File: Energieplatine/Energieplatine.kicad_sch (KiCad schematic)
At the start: 22 parts, among them J1 USB_C_Receptacle_PowerOnly_6P, J2 Conn_01x02_Pin, U1 4027, U2 TL072, U3 LM2576HVT-ADJ, U4 LM2577T-ADJ

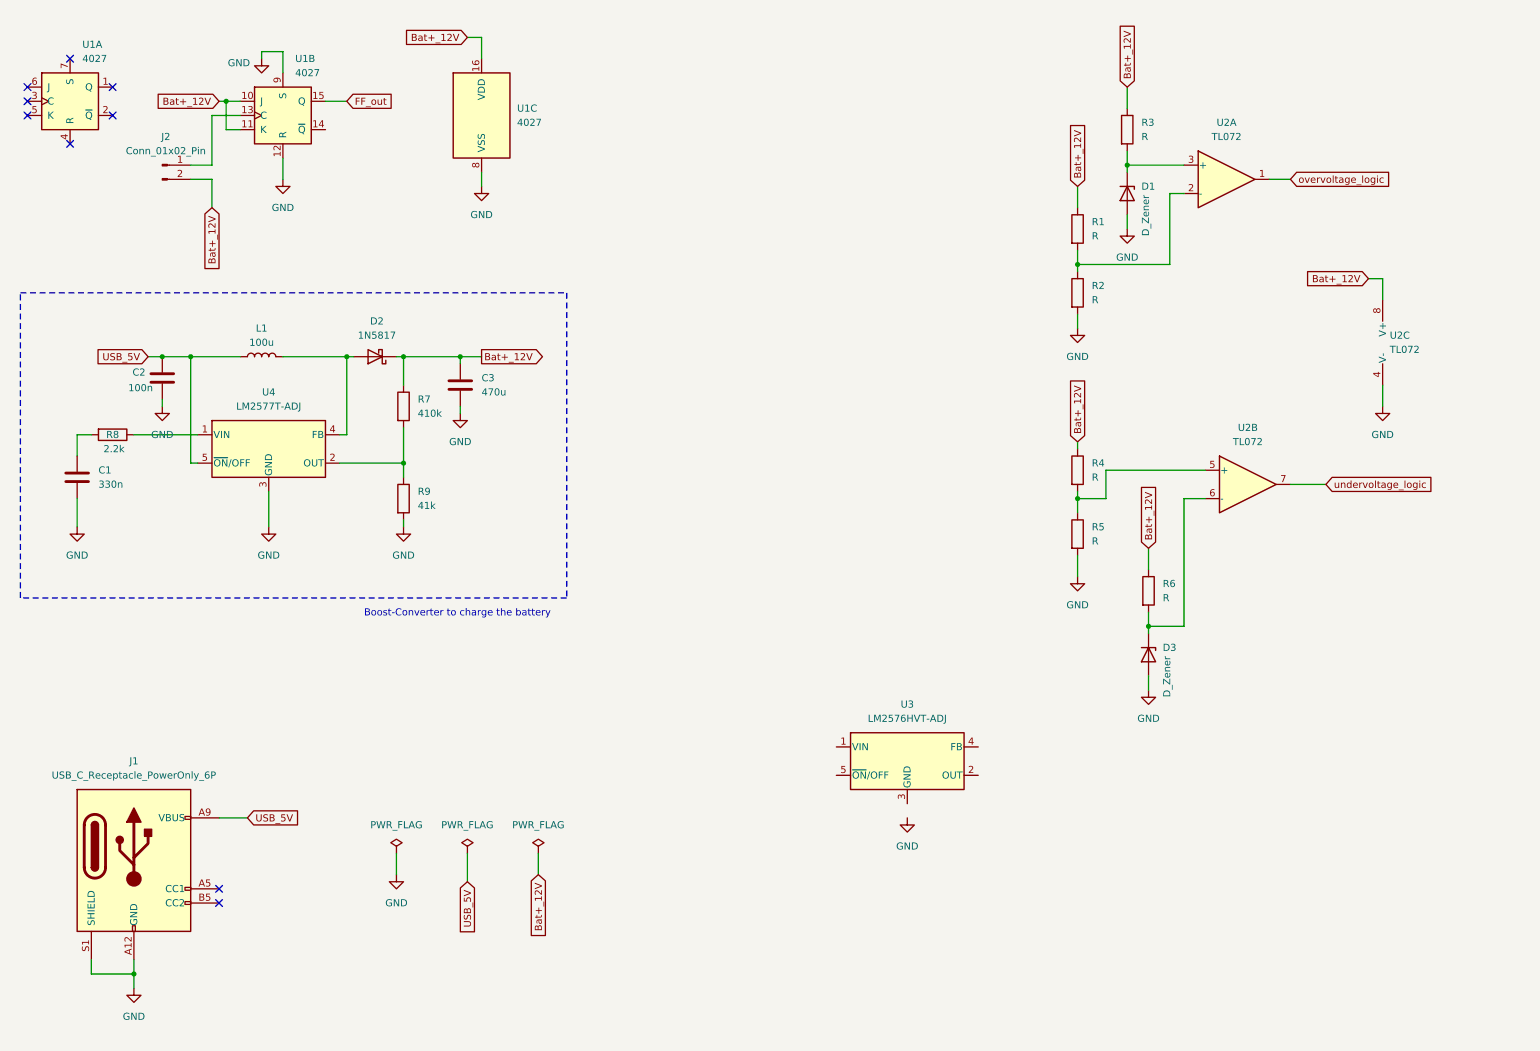
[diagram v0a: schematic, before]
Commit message: Layout is has no DRC errors.
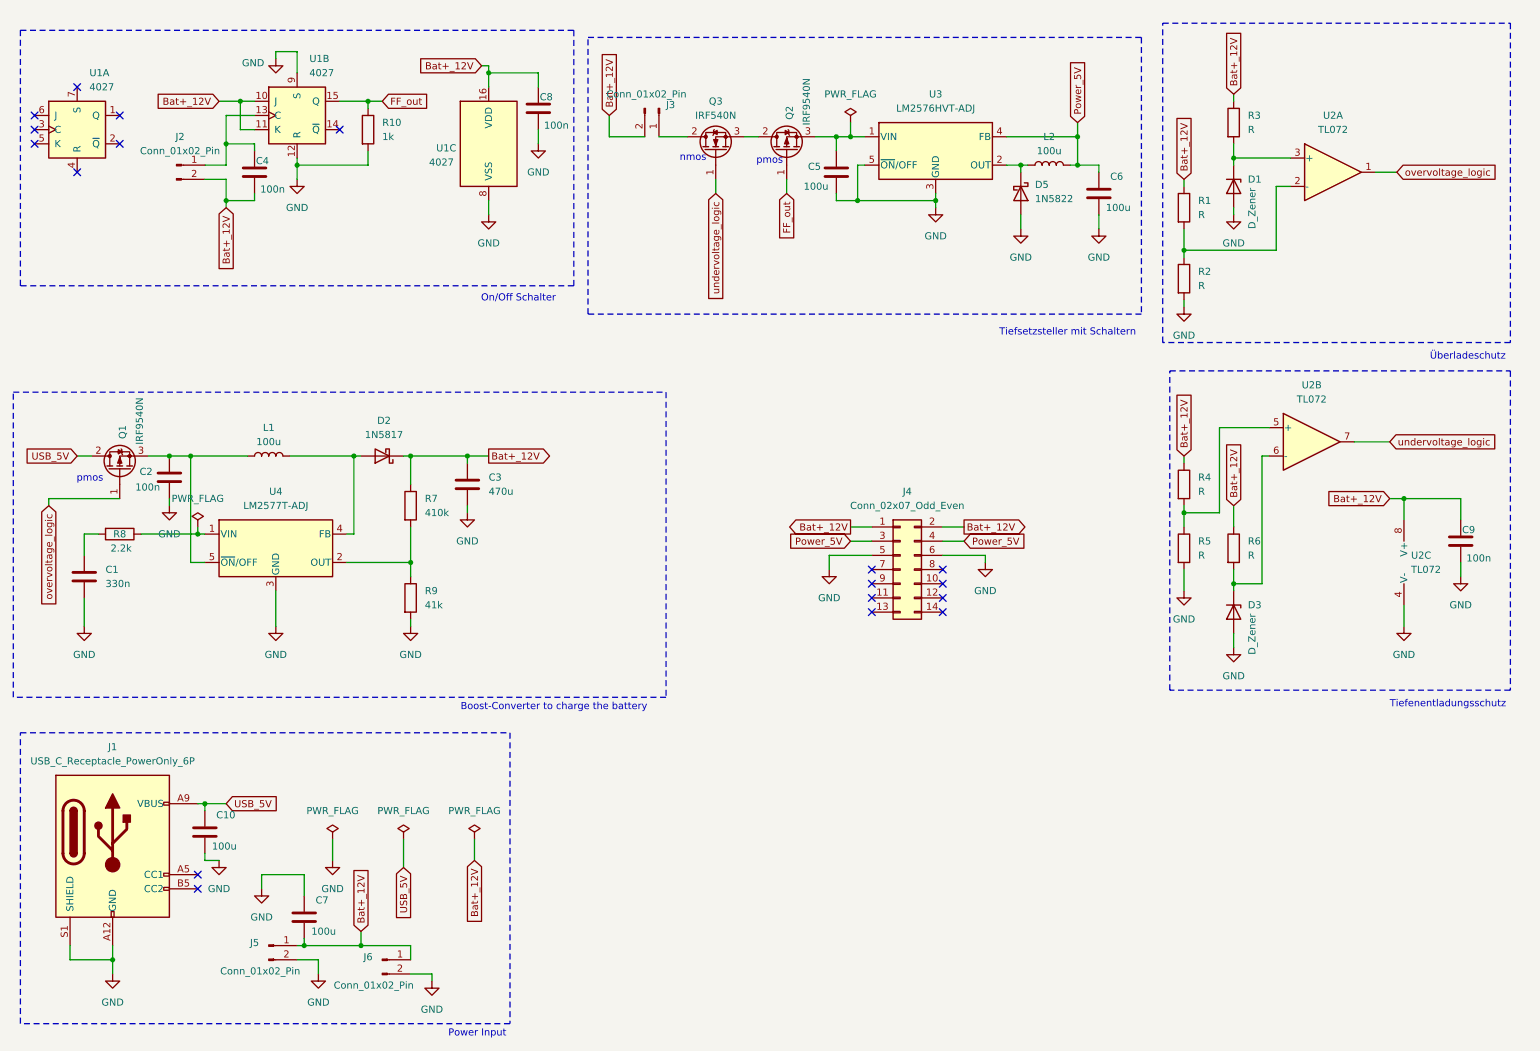
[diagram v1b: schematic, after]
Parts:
- added C10, C5, C6, C7: 100u, Capacitor_THT:C_Radial_D6.3mm_H11.0mm_P2.50mm, symbol Device:C
- added C4, C8, C9: 100n, Capacitor_THT:C_Disc_D5.0mm_W2.5mm_P2.50mm, symbol Device:C
- added D5: 1N5822, Diode_THT:D_DO-41_SOD81_P10.16mm_Horizontal, symbol Diode:1N5822
- added J3, J5, J6: Conn_01x02_Pin, Connector_PinHeader_2.00mm:PinHeader_1x02_P2.00mm_Vertical, symbol Connector:Conn_01x02_Pin
- added J4: Conn_02x07_Odd_Even, Projektlabor:Prolab_Busstecker, symbol Connector_Generic:Conn_02x07_Odd_Even
- added L2: 100u, Inductor_THT:L_Radial_D6.0mm_P4.00mm, symbol Device:L
- added Q1, Q2: IRF9540N, Package_TO_SOT_THT:TO-220-3_Vertical, symbol Transistor_FET:IRF9540N
- added Q3: IRF540N, Package_TO_SOT_THT:TO-220-3_Vertical, symbol Transistor_FET:IRF540N
- added R10: 1k, Resistor_THT:R_Axial_DIN0309_L9.0mm_D3.2mm_P12.70mm_Horizontal, symbol Device:R
- C1, C2: footprint (none) -> Capacitor_THT:C_Disc_D5.0mm_W2.5mm_P2.50mm
- C3: footprint (none) -> Capacitor_THT:C_Radial_D8.0mm_H11.5mm_P3.50mm
- D1, D3: footprint Diode_THT:D_DO-27_P12.70mm_Horizontal -> Diode_THT:D_A-405_P10.16mm_Horizontal
- J2: footprint Connector:JWT_A3963_1x02_P3.96mm_Vertical -> Connector_PinHeader_2.00mm:PinHeader_1x02_P2.00mm_Vertical
- L1: footprint (none) -> Inductor_THT:L_Radial_D6.0mm_P4.00mm
- R1, R2, R3, R4, R5, R6: footprint Resistor_THT:R_Axial_DIN0207_L6.3mm_D2.5mm_P5.08mm_Vertical -> Resistor_THT:R_Axial_DIN0309_L9.0mm_D3.2mm_P12.70mm_Horizontal
- R7, R8, R9: footprint (none) -> Resistor_THT:R_Axial_DIN0309_L9.0mm_D3.2mm_P12.70mm_Horizontal
- U3, U4: footprint Package_TO_SOT_THT:TO-220-5_Vertical -> Projektlabor:TO-220-5_Vertical_Brolab
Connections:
- net Bat+_12V: now also C4.2, C7.2, C8.1, C9.1, J3.2 (Pin_2), J4.1 (Pin_1), J4.2 (Pin_2), J5.1 (Pin_1), J6.1 (Pin_1)
- net FF_out: now also Q2.1 (G), R10.1
- net GND: now also U3.3 (GND), U3.5 (~{ON}/OFF), C10.2, C5.2, C6.2, C7.1, C8.2, C9.2, D5.2 (A), J4.5 (Pin_5), J4.6 (Pin_6), J5.2 (Pin_2), J6.2 (Pin_2), R10.2
- net USB_5V: now also C10.1, Q1.2 (D); no longer C2.1, L1.1, U4.5 (~{ON}/OFF)
- net overvoltage_logic: now also Q1.1 (G)
- net undervoltage_logic: now also Q3.1 (G)
- net at U3.1 (VIN): now also C5.1, Q2.3 (S)
- net at U3.2 (OUT): now also D5.1 (K), L2.1
- net Power_5V: now reaches U3.4 (FB)
- net Power_5V: now also C6.1, J4.3 (Pin_3), J4.4 (Pin_4), L2.2
- net at J2.1 (Pin_1), U1.13 (C): now also C4.1
- new net: C2.1, L1.1, Q1.3 (S), U4.5 (~{ON}/OFF)
- new net: J3.1 (Pin_1), Q3.2 (D)
- new net: Q2.2 (D), Q3.3 (S)
- no-connect marks 9 -> 18
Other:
- note added: "On/Off Schalter"
- note added: "Power Input"
- note added: "Tiefenentladungsschutz"
- note added: "Tiefsetzsteller mit Schaltern"
- note added: "nmos"
- note added: "pmos"
- note added: "Überladeschutz"
- moved on the sheet: C1, C2, C3, D1, D2, D3, J1, J2, L1, R1, R2, R3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

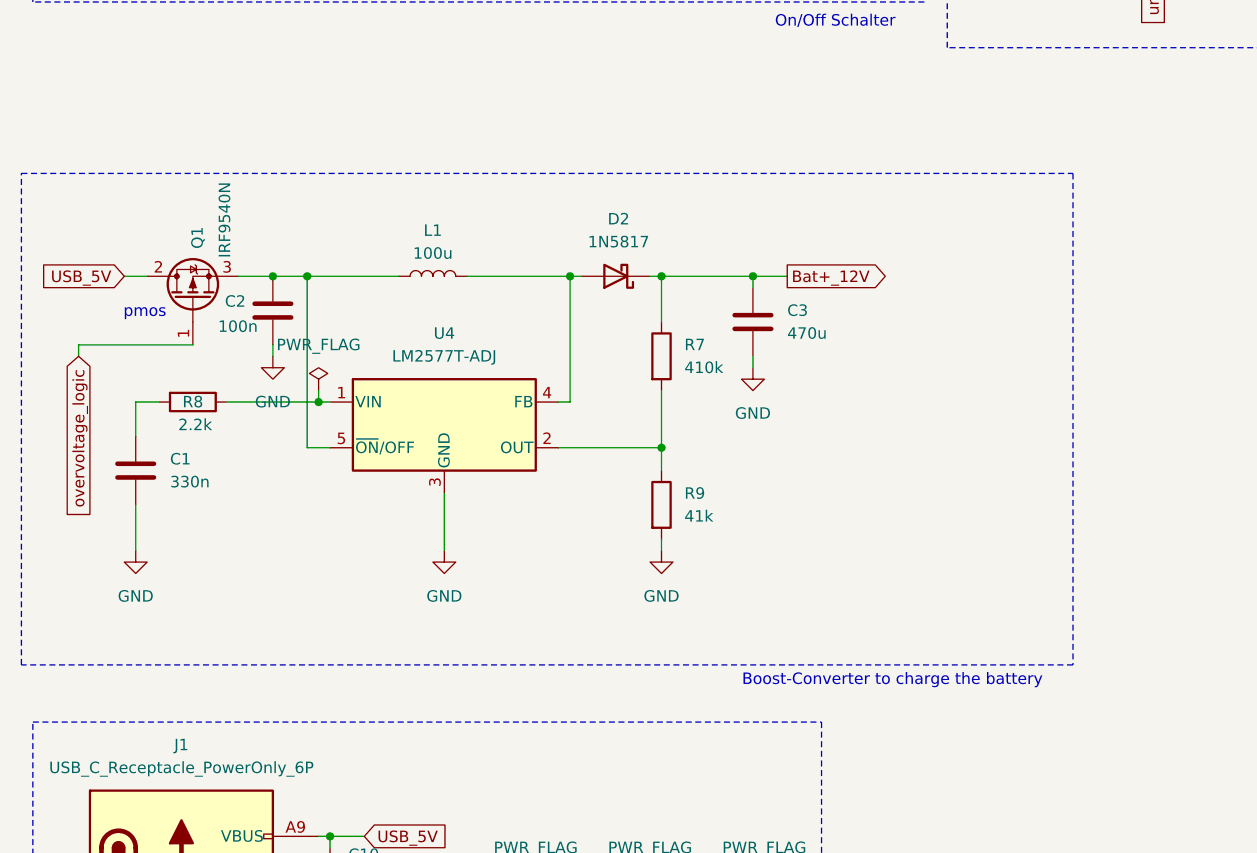
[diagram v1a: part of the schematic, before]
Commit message: PCB updated
Footprints der Widerstände angepasst, daraufhin Layout der Platine angepasst.
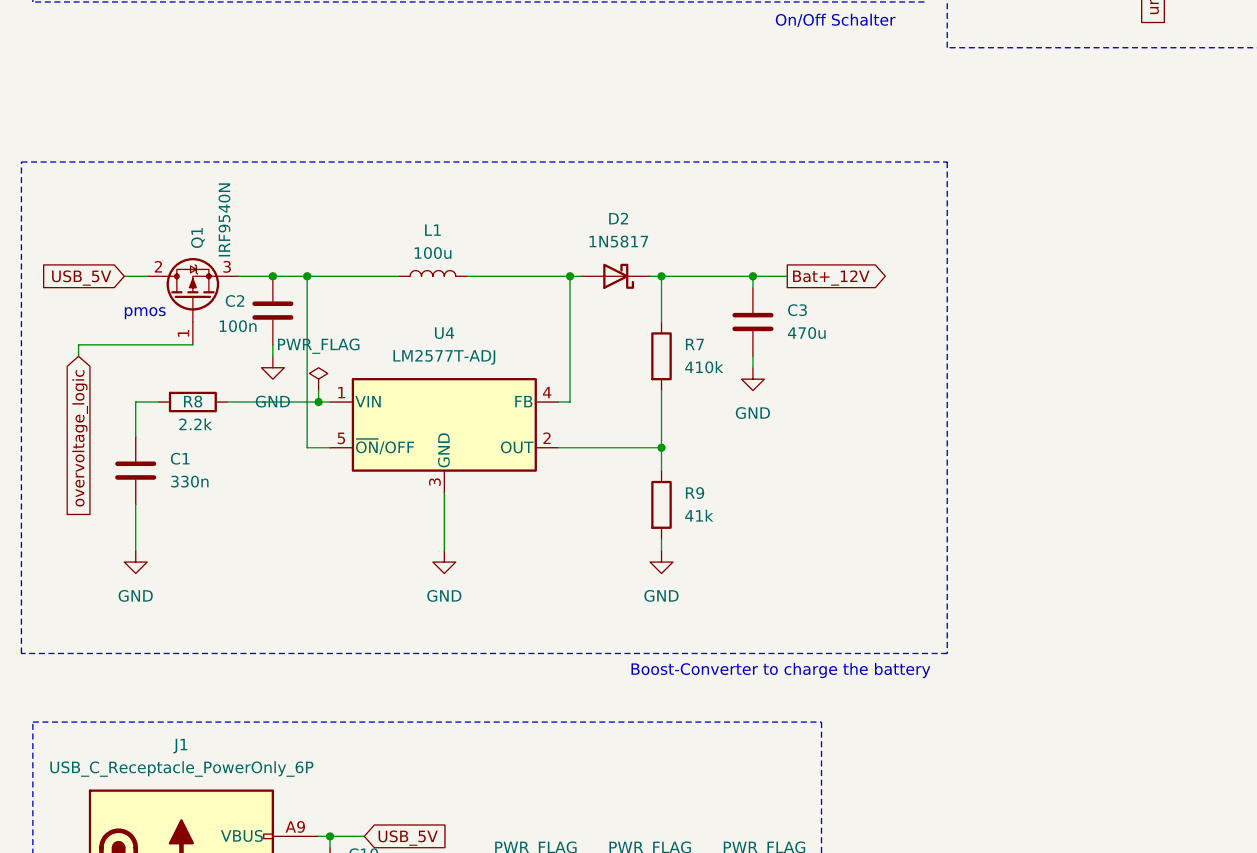
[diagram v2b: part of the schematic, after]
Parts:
- R1, R10, R2, R3, R4, R5, R6, R7, R8, R9: footprint Resistor_THT:R_Axial_DIN0309_L9.0mm_D3.2mm_P12.70mm_Horizontal -> Resistor_THT:R_Axial_DIN0207_L6.3mm_D2.5mm_P7.62mm_Horizontal
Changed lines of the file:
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@@
 	)
 	(rectangle
-		(start 15.24 78.74)
-		(end 132.08 133.35)
+		(start 15.24 77.47)
+		(end 118.11 132.08)
 		(stroke
-			(width 0.0508)
+			(width 0)
 			(type dash)
-			(color 146 167 255 1)
 		)
 		(fill
@@
 	(text "Boost-Converter to charge the battery"
 		(exclude_from_sim no)
-		(at 112.014 135.128 0)
+		(at 99.568 134.112 0)
 		(effects
 			(font
@@
 			)
 		)
-		(property "Footprint" "Resistor_THT:R_Axial_DIN0309_L9.0mm_D3.2mm_P12.70mm_Horizontal"
+		(property "Footprint" "Resistor_THT:R_Axial_DIN0207_L6.3mm_D2.5mm_P7.62mm_Horizontal"
 			(at 34.29 102.362 90)
 			(effects
@@
 			)
 		)
-		(property "Footprint" "Resistor_THT:R_Axial_DIN0309_L9.0mm_D3.2mm_P12.70mm_Horizontal"
+		(property "Footprint" "Resistor_THT:R_Axial_DIN0207_L6.3mm_D2.5mm_P7.62mm_Horizontal"
 			(at 231.902 30.48 90)
 			(effects
@@
 			)
 		)
-		(property "Footprint" "Resistor_THT:R_Axial_DIN0309_L9.0mm_D3.2mm_P12.70mm_Horizontal"
+		(property "Footprint" "Resistor_THT:R_Axial_DIN0207_L6.3mm_D2.5mm_P7.62mm_Horizontal"
 			(at 223.012 106.68 90)
 			(effects
@@
 			)
 		)
-		(property "Footprint" "Resistor_THT:R_Axial_DIN0309_L9.0mm_D3.2mm_P12.70mm_Horizontal"
+		(property "Footprint" "Resistor_THT:R_Axial_DIN0207_L6.3mm_D2.5mm_P7.62mm_Horizontal"
 			(at 84.582 115.57 90)
 			(effects
@@
 			)
 		)
-		(property "Footprint" "Resistor_THT:R_Axial_DIN0309_L9.0mm_D3.2mm_P12.70mm_Horizontal"
+		(property "Footprint" "Resistor_THT:R_Axial_DIN0207_L6.3mm_D2.5mm_P7.62mm_Horizontal"
 			(at 223.012 45.72 90)
 			(effects
@@
 			)
 		)
-		(property "Footprint" "Resistor_THT:R_Axial_DIN0309_L9.0mm_D3.2mm_P12.70mm_Horizontal"
+		(property "Footprint" "Resistor_THT:R_Axial_DIN0207_L6.3mm_D2.5mm_P7.62mm_Horizontal"
 			(at 84.582 99.06 90)
 			(effects
@@
 			)
 		)
-		(property "Footprint" "Resistor_THT:R_Axial_DIN0309_L9.0mm_D3.2mm_P12.70mm_Horizontal"
+		(property "Footprint" "Resistor_THT:R_Axial_DIN0207_L6.3mm_D2.5mm_P7.62mm_Horizontal"
 			(at 223.012 58.42 90)
 			(effects
@@
 			)
 		)
-		(property "Footprint" "Resistor_THT:R_Axial_DIN0309_L9.0mm_D3.2mm_P12.70mm_Horizontal"
+		(property "Footprint" "Resistor_THT:R_Axial_DIN0207_L6.3mm_D2.5mm_P7.62mm_Horizontal"
 			(at 76.962 31.75 90)
 			(effects
@@
 			)
 		)
-		(property "Footprint" "Resistor_THT:R_Axial_DIN0309_L9.0mm_D3.2mm_P12.70mm_Horizontal"
+		(property "Footprint" "Resistor_THT:R_Axial_DIN0207_L6.3mm_D2.5mm_P7.62mm_Horizontal"
 			(at 223.012 95.25 90)
 			(effects
@@
 			)
 		)
-		(property "Footprint" "Resistor_THT:R_Axial_DIN0309_L9.0mm_D3.2mm_P12.70mm_Horizontal"
+		(property "Footprint" "Resistor_THT:R_Axial_DIN0207_L6.3mm_D2.5mm_P7.62mm_Horizontal"
 			(at 231.902 106.68 90)
 			(effects
